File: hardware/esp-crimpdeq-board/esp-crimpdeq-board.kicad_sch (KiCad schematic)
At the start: 72 parts, among them J1 USB4105-GF-A, J2 Conn_01x02_Pin, Q1 DMG3415U, SW1 SW_Push, SW2 SW_Push, U1 SHTC3, U2 ICM-42670-P, U3 REF35330QDBVR, U4 SY8088, U5 NAU7802SGI, U6 MCP73831T-2ACI/OT, U7 MAX17262, U8 ESP32-C6-MINI-1/U, Y1 32.768Hz

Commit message: Update esp-crimpdeq-board.kicad_sch
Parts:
- removed U5: NAU7802SGI, Package_SO:SOP-16_3.9x9.9mm_P1.27mm, symbol Nuvoton:NAU7802SGI
- added C26: 1uF 16V, Capacitor_SMD:C_0402_1005Metric, symbol Device:C_Small
- added C27: 0.1uF 10V, Capacitor_SMD:C_0402_1005Metric, symbol Device:C_Small
- added C28: 10uF 16V, Capacitor_SMD:C_0805_2012Metric, symbol Device:C_Small
- added J3: Conn_01x04_Pin, Connector_PinHeader_1.27mm:PinHeader_1x04_P1.27mm_Vertical, symbol Connector:Conn_01x04_Pin
- added U5: NAU7802SGI, Package_SO:SOP-16_3.9x9.9mm_P1.27mm, symbol PCM_Nuvoton:NAU7802SGI
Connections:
- net +3V3: now also C26.1, U5.15 (DVDD)
- net GND: now also C26.2, C27.2, C28.2, J3.4 (Pin_4), U5.7 (REFN), U5.8 (AVSS), U5.9 (DVSS)
- net IO3_SDA: no longer R18.2, U2.14 (AP_SDA/AP_SDIO/AP_SDI)
- net IO4_SCL: no longer R17.2, U2.13 (AP_SCL/AP_SCLK)
- net VREF3V3: now also J3.1 (Pin_1), U5.1 (REFP)
- net at C21.1: now also U5.6 (VBG)
- net at C19.1: now also U5.5 (VIN2P)
- net at C19.2: now also U5.4 (VIN2N)
- net at R13.1: now also J3.3 (Pin_3)
- net at C20.2, R13.2: now also U5.2 (VIN1N)
- net at U3.5 (NR): now also C28.1
- net at C20.1, R10.2: now also U5.3 (VIN1P)
- net at R10.1: now also J3.2 (Pin_2)
- net IO2 renamed RGB_LED_PIN
- net IO5 renamed CHARGING
- new net: C27.1, U5.16 (AVDD/LDO)
- new net DRDY: U5.12 (DRDY)
- new net IOX_SCL: R17.2, U2.13 (AP_SCL/AP_SCLK), U5.13 (SCLK)
- new net IOX_SDA: R18.2, U2.14 (AP_SDA/AP_SDIO/AP_SDI), U5.14 (SDIO)
- no-connect marks 5 -> 7
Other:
- note added: "LED RGB"
- note removed: "LED Addressable on GPIO2 to show status"
- moved on the sheet: C19, C20, C21, C22, C23, C24, C25, D5, D6, D7, D8, D9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

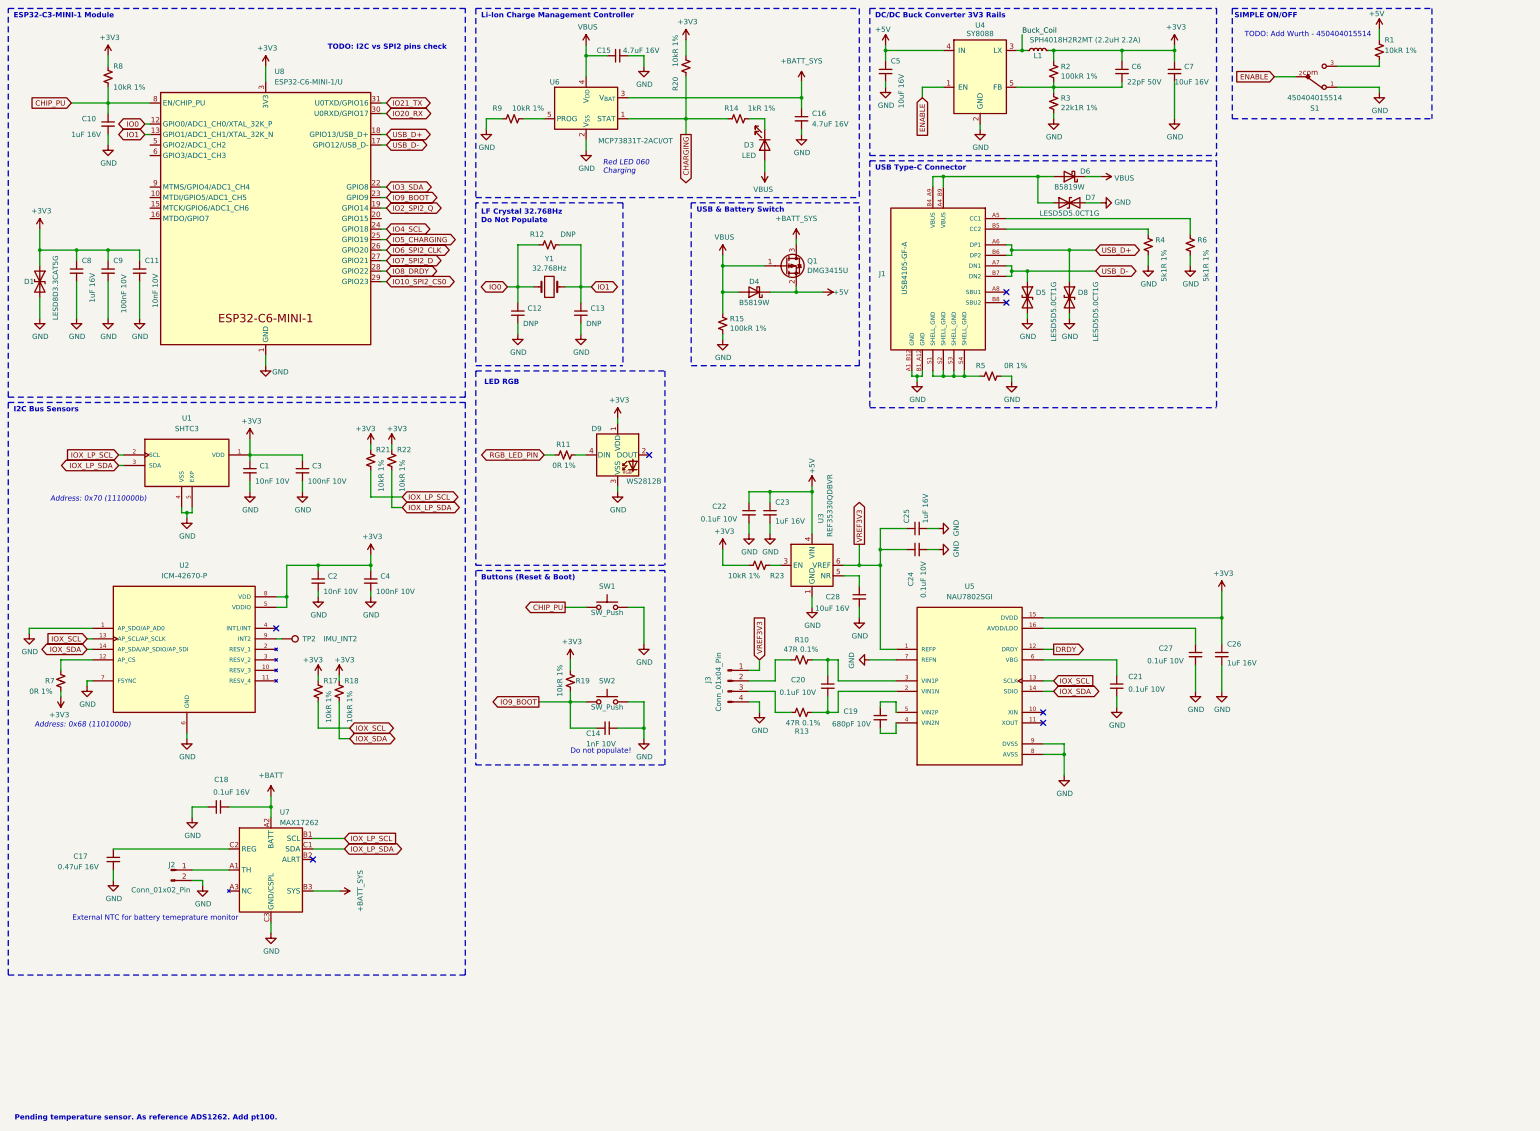
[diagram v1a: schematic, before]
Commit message: Schematic ready to review. Pending some footprints. Pending to add PN.
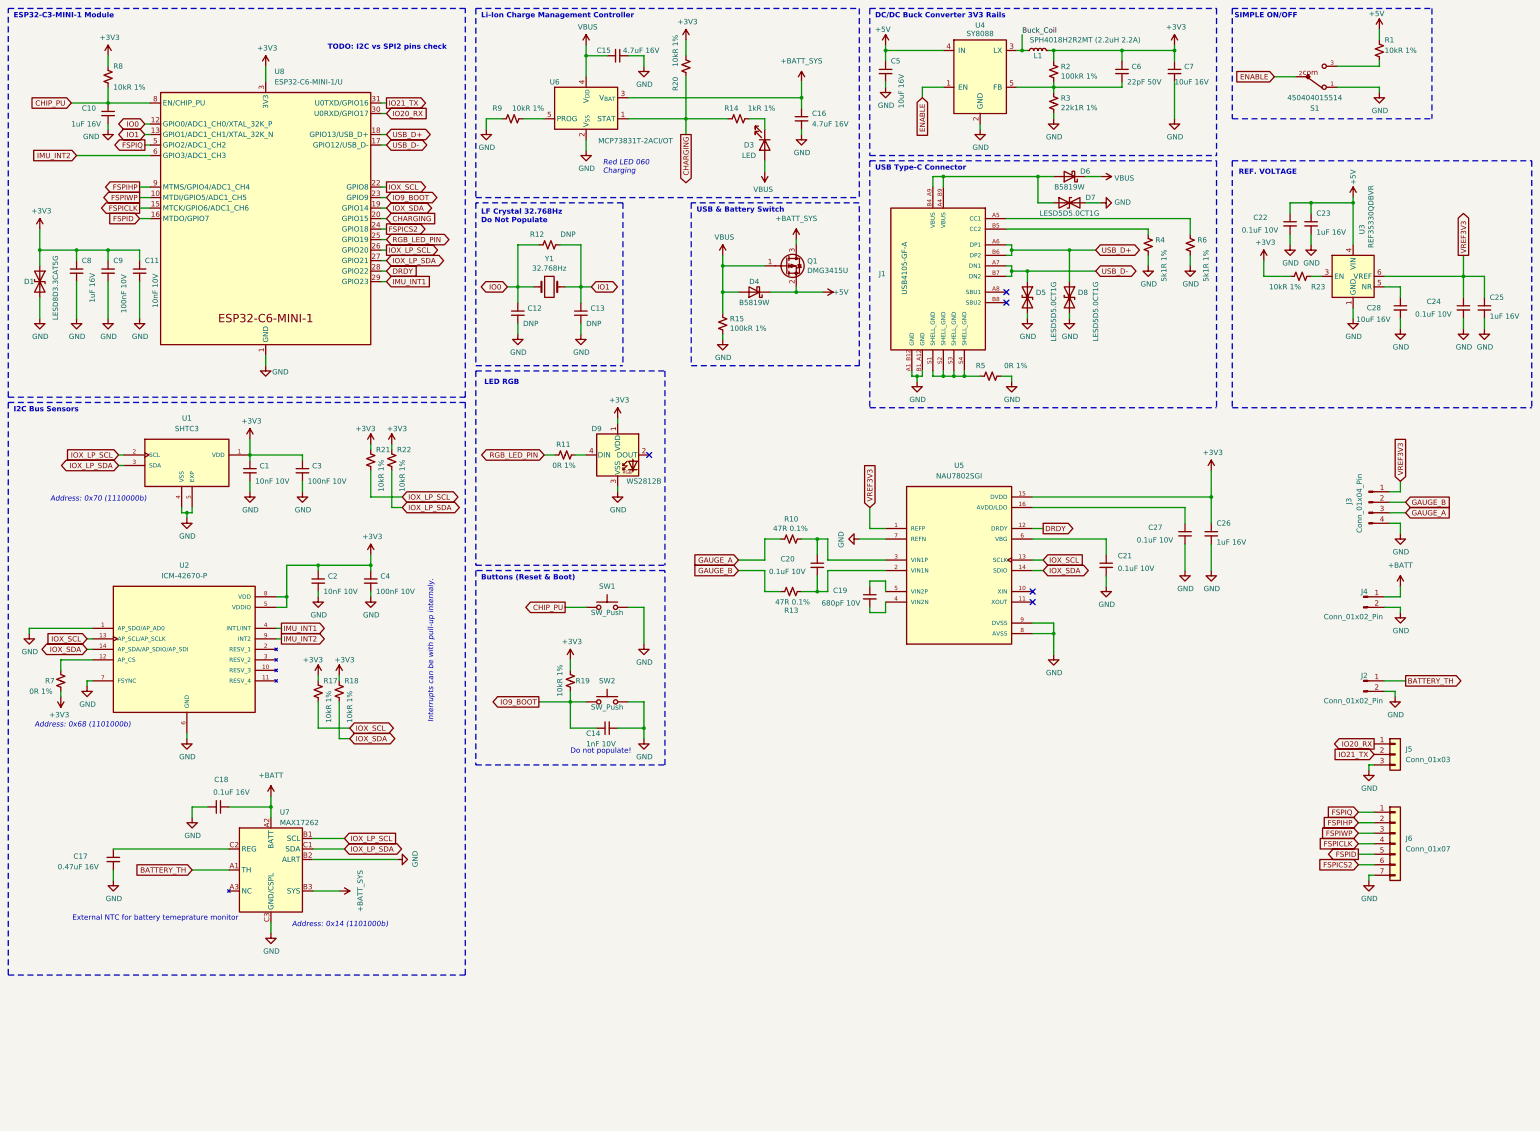
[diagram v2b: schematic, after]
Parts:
- removed TP2: IMU_INT2, TestPoint:TestPoint_Pad_D1.0mm, symbol Connector:TestPoint
- added J4: Conn_01x02_Pin, symbol Connector:Conn_01x02_Pin
- added J5: Conn_01x03, symbol Connector_Generic:Conn_01x03
- added J6: Conn_01x07, symbol Connector_Generic:Conn_01x07
- D1: footprint Rust_Board:SOD-882 -> Diode_SMD:D_SOD-882
- J3: footprint Connector_PinHeader_1.27mm:PinHeader_1x04_P1.27mm_Vertical -> Connector_PinHeader_1.27mm:PinHeader_1x02_P1.27mm_Vertical
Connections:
- net IO10_SPI2_CS0 is gone; now on net IMU_INT1: U8.29 (GPIO23)
- net IO2_SPI2_Q is gone; now on net IOX_SDA: U8.19 (GPIO14)
- net IO3_SDA is gone; now on net IOX_SCL: U8.22 (GPIO8)
- net IO5_CHARGING is gone; now on net RGB_LED_PIN: U8.25 (GPIO19)
- net IO6_SPI2_CLK is gone; now on net IOX_LP_SCL: U8.26 (GPIO20)
- net IO7_SPI2_D is gone; now on net IOX_LP_SDA: U8.27 (GPIO21)
- net IO8_DRDY is gone; now on net DRDY: U8.28 (GPIO22)
- net +BATT: now also J4.1 (Pin_1)
- net CHARGING: now also U8.20 (GPIO15)
- net GND: now also U7.B2 (ALRT), J4.2 (Pin_2), J5.3 (Pin_3), J6.7 (Pin_7)
- net IO20_RX: now also J5.1 (Pin_1)
- net IO21_TX: now also J5.2 (Pin_2)
- net IMU_INT2: now reaches U2.9 (INT2)
- net IMU_INT2: now also U8.6 (GPIO3/ADC1_CH3)
- net IMU_INT1: now reaches U2.4 (INT1/INT)
- net BATTERY_TH: now reaches J2.1 (Pin_1), U7.A1 (TH)
- net FSPIWP: now reaches U8.10 (MTDI/GPIO5/ADC1_CH5)
- net FSPIWP: now also J6.3 (Pin_3)
- net FSPICLK: now reaches U8.15 (MTCK/GPIO6/ADC1_CH6)
- net FSPICLK: now also J6.4 (Pin_4)
- net FSPID: now reaches U8.16 (MTDO/GPIO7)
- net FSPID: now also J6.5 (Pin_5)
- net FSPIQ: now reaches U8.5 (GPIO2/ADC1_CH2)
- net FSPIQ: now also J6.1 (Pin_1)
- net FSPIHP: now reaches U8.9 (MTMS/GPIO4/ADC1_CH4)
- net FSPIHP: now also J6.2 (Pin_2)
- net GAUGE_A: now reaches R10.1
- net GAUGE_A: now also J3.3 (Pin_3); no longer J3.2 (Pin_2)
- net GAUGE_B: now reaches R13.1
- net GAUGE_B: now also J3.2 (Pin_2); no longer J3.3 (Pin_3)
- net IO4_SCL renamed FSPICS2
- net FSPICS2: now also J6.6 (Pin_6)
- no-connect marks 7 -> 5
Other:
- note added: "Address: 0x14 (1101000b)"
- note added: "Interrupts can be with pull-up internaly."
- note added: "REF. VOLTAGE"
- note removed: "Pending temperature sensor. As reference ADS1262. Add pt100."
- note removed: "TODO: Add Wurth - 450404015514"
- moved on the sheet: C10, C19, C20, C21, C22, C23, C24, C25, C26, C27, C28, J2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

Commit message: Final schematic
Pending footprints. Review battery connector pins.
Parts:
- removed C21, C27: 0.1uF 10V, Capacitor_SMD:C_0402_1005Metric, symbol Device:C_Small
- removed C26: 1uF 16V, Capacitor_SMD:C_0402_1005Metric, symbol Device:C_Small
- removed J4: Conn_01x02_Pin, symbol Connector:Conn_01x02_Pin
- removed J5: Conn_01x03, symbol Connector_Generic:Conn_01x03
- removed J6: Conn_01x07, symbol Connector_Generic:Conn_01x07
- removed R10, R13: 47R 0.1%, Resistor_SMD:R_0402_1005Metric, symbol Device:R_Small_US
- removed U5: NAU7802SGI, Package_SO:SOP-16_3.9x9.9mm_P1.27mm, symbol PCM_Nuvoton:NAU7802SGI
- added C29, C30, C31: 0.1uF 10V, Capacitor_SMD:C_0402_1005Metric, symbol Device:C_Small
- added IC3: ADS1230IPWR, Package_SO:TSSOP-16_4.4x5mm_P0.65mm, symbol PCM_Texas_Instruments:ADS1230IPWR
- added J4: Conn_01x08_Pin, Connector_PinHeader_1.27mm:PinHeader_1x08_P1.27mm_Vertical, symbol Connector:Conn_01x08_Pin
- added J5: Conn_01x02, symbol Connector_Generic:Conn_01x02
- added R16: 10kR 1%, Resistor_SMD:R_0402_1005Metric, symbol Device:R_Small_US
- C19: value 680pF 10V -> 10nF 10V
- C20: value 0.1uF 10V -> 100nF 10V; LCSC C15195 -> C1525
- J2: footprint (none) -> Connector_PinHeader_1.27mm:PinHeader_1x02_P1.27mm_Vertical
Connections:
- net +3V3: now also C19.1, C20.1, IC3.1 (DVDD), J4.2 (Pin_2), R16.1
- net +BATT: now also J5.2 (Pin_2)
- net FSPICLK: now also U8.26 (GPIO20), J4.5 (Pin_5); no longer U8.15 (MTCK/GPIO6/ADC1_CH6)
- net FSPICS2: now also J4.3 (Pin_3)
- net FSPID: now also U8.27 (GPIO21), J4.4 (Pin_4); no longer U8.16 (MTDO/GPIO7)
- net FSPIHP: now also J4.7 (Pin_7)
- net FSPIQ: now also J4.8 (Pin_8)
- net FSPIWP: now also J4.6 (Pin_6)
- net GAUGE_A: now also J3.2 (Pin_2), IC3.7 (AINP); no longer J3.3 (Pin_3)
- net GAUGE_B: now also J3.3 (Pin_3), IC3.8 (AINN); no longer J3.2 (Pin_2)
- net GND: now also C19.2, C20.2, C29.2, C30.2, IC3.11 (AGND), IC3.2 (DGND), IC3.3 (CLKIN), IC3.9 (REFN), J4.1 (Pin_1), J5.1 (Pin_1)
- net IO9_BOOT: now also IC3.15 (SCLK)
- net IOX_LP_SCL: now also U8.16 (MTDO/GPIO7); no longer U8.26 (GPIO20)
- net IOX_LP_SDA: now also U8.15 (MTCK/GPIO6/ADC1_CH6); no longer U8.27 (GPIO21)
- net VREF3V3: now also C29.1, C30.1, IC3.10 (REFP), IC3.12 (AVDD)
- net DRDY renamed SERIALDATA
- net SERIALDATA: now also IC3.16 (~{DRDY}/DOUT)
- net IO20_RX renamed RESET_ADC
- net RESET_ADC: now also IC3.14 (~{PDWN})
- net IO21_TX renamed ADC_GAIN
- net ADC_GAIN: now also IC3.4 (GAIN)
- new net: C31.1, IC3.5 (CAP_1)
- new net: C31.2, IC3.6 (CAP_2)
- new net: IC3.13 (SPEED), R16.2
- no-connect marks 5 -> 3
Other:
- note added: "High speed option"

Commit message: feat: Rename pins and reorganize
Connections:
- net ADC_GAIN renamed ADC1_GAIN
- net IO9_BOOT renamed BOOT_ADC1_CLK
- net IOX_LP_SCL renamed LP_SCL
- net IOX_LP_SDA renamed LP_SDA
- net IOX_SCL renamed SCL
- net IOX_SDA renamed SDA
- net RESET_ADC renamed ADC1_RESET
- net SERIALDATA renamed ADC1_DATA
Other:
- note added: "ADC1 (ADS1230)"
- note added: "ESP32-C6-MINI-1 Module"
- note added: "External connectors"
- note removed: "ESP32-C3-MINI-1 Module"
- moved on the sheet: R16

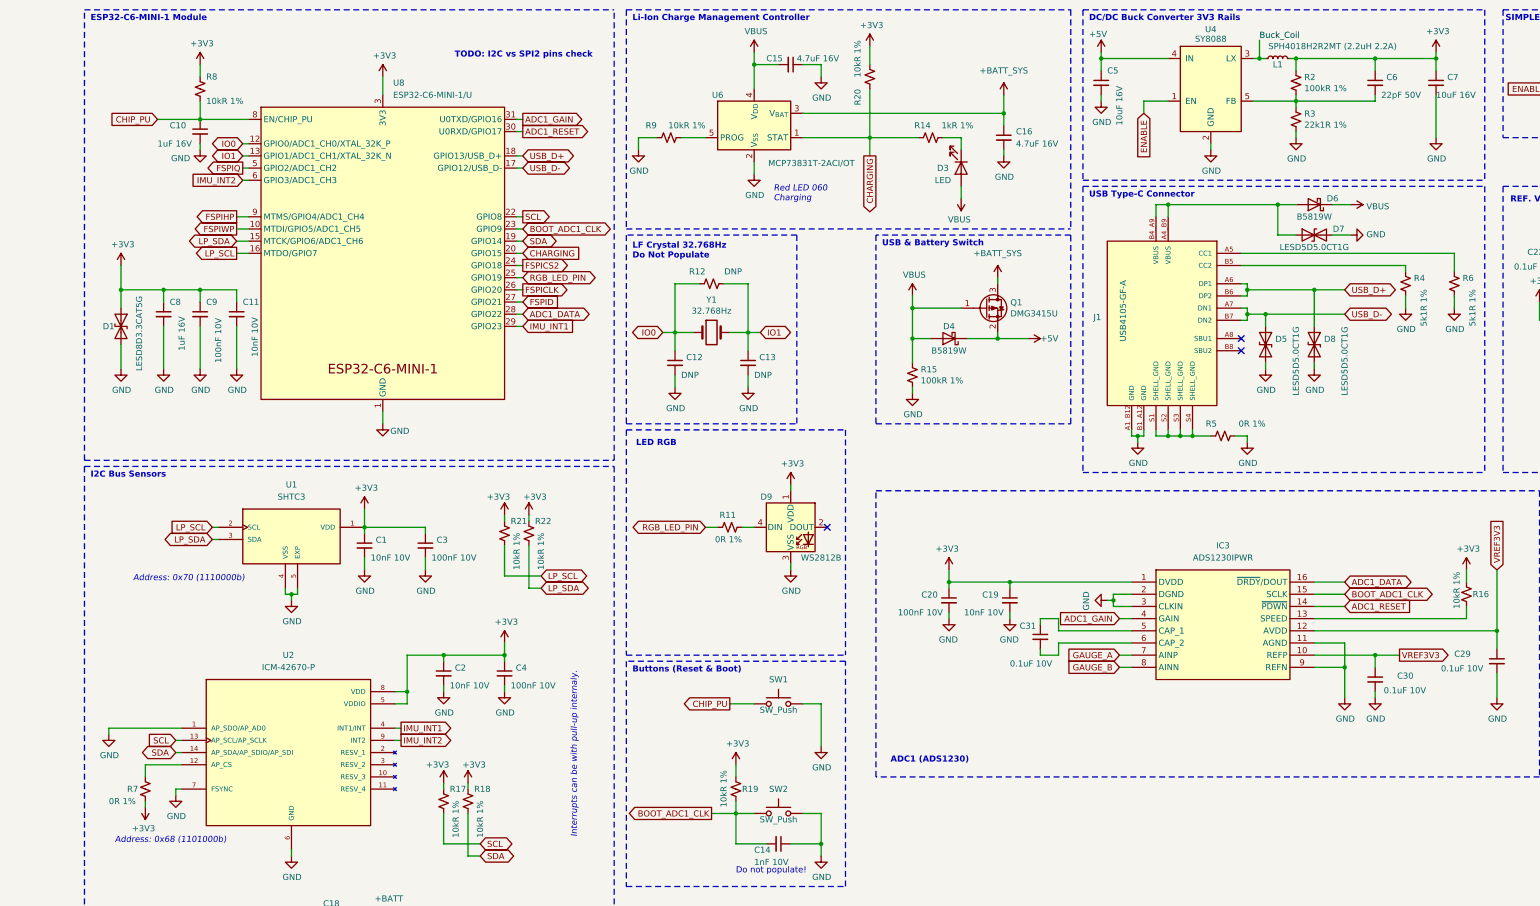
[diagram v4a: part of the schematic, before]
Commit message: Update esp-crimpdeq-board.kicad_sch
Minor pinout change
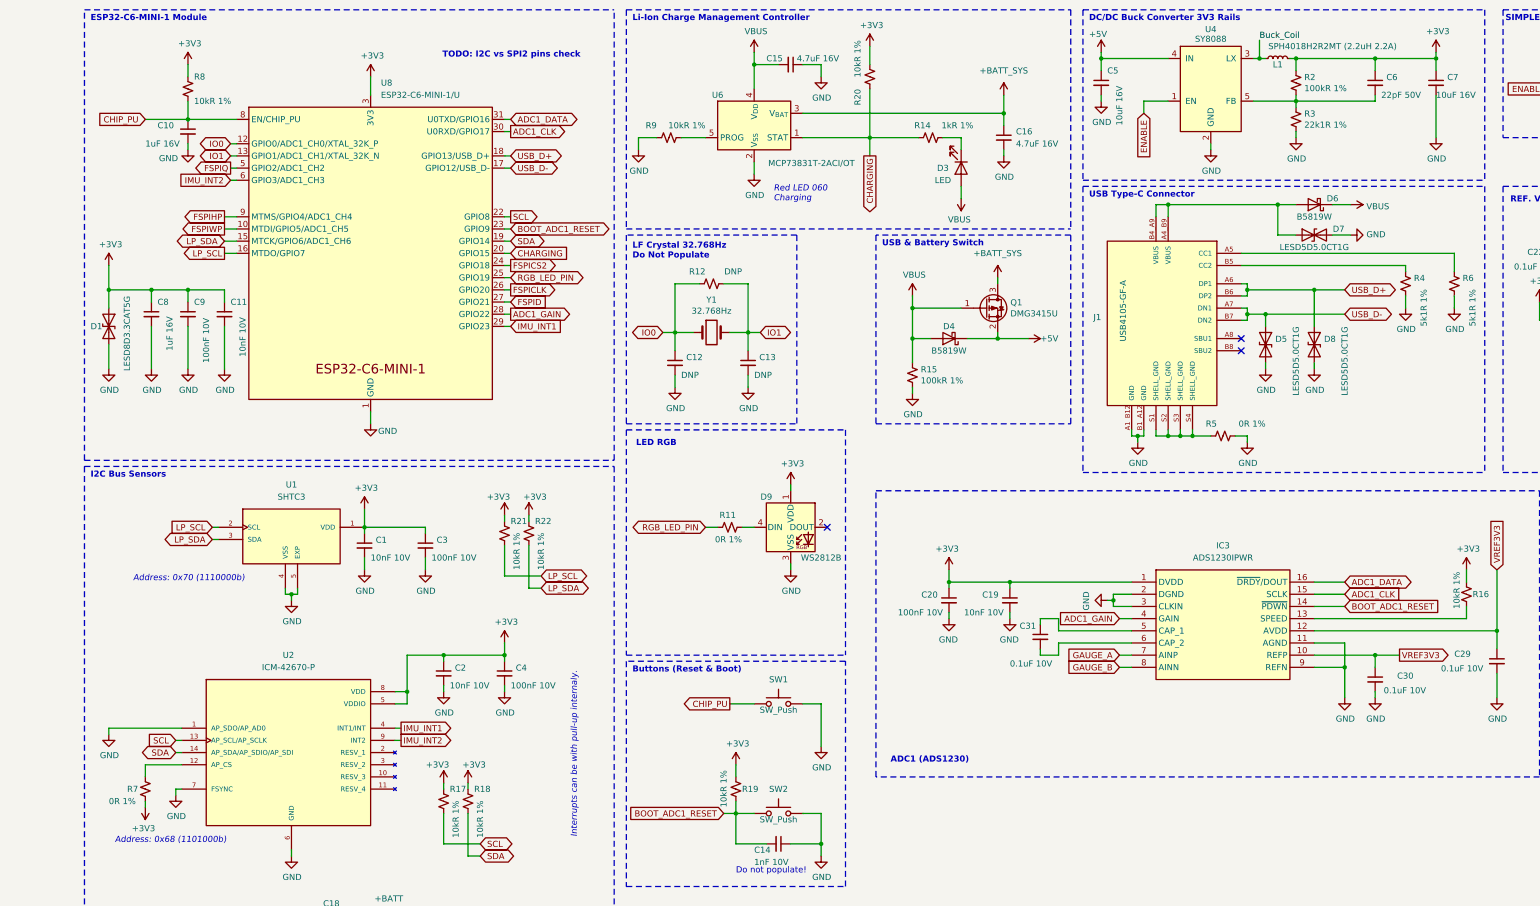
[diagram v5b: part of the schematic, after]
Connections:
- net ADC1_DATA: now also U8.31 (U0TXD/GPIO16); no longer U8.28 (GPIO22)
- net ADC1_GAIN: now also U8.28 (GPIO22); no longer U8.31 (U0TXD/GPIO16)
- net ADC1_RESET renamed ADC1_CLK
- net ADC1_CLK: now also IC3.15 (SCLK); no longer IC3.14 (~{PDWN})
- net BOOT_ADC1_CLK renamed BOOT_ADC1_RESET
- net BOOT_ADC1_RESET: now also IC3.14 (~{PDWN}); no longer IC3.15 (SCLK)
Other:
- moved on the sheet: C10, C11, C8, C9, D1, R8, U8
